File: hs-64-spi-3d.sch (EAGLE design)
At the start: 30 parts, among them J1 DF40C-70DP-0.4V(51), J2 A79622-001, U1 RHD2064_BGA, U2 BNO055, U3 TLV70725

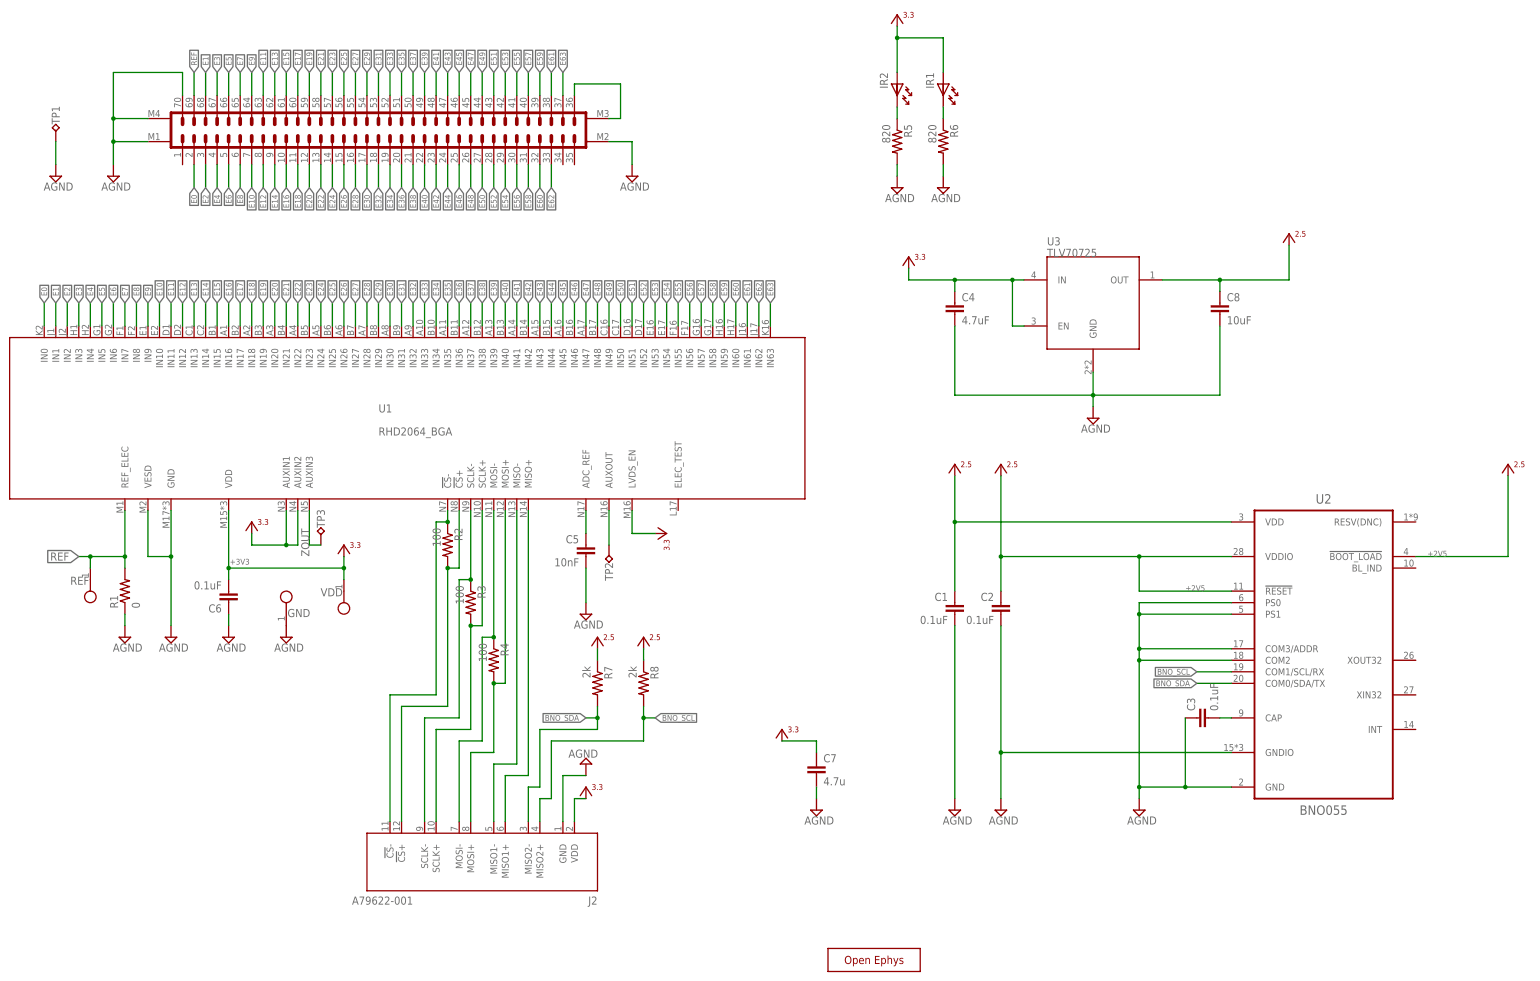
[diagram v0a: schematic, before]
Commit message: Added EEPROM.
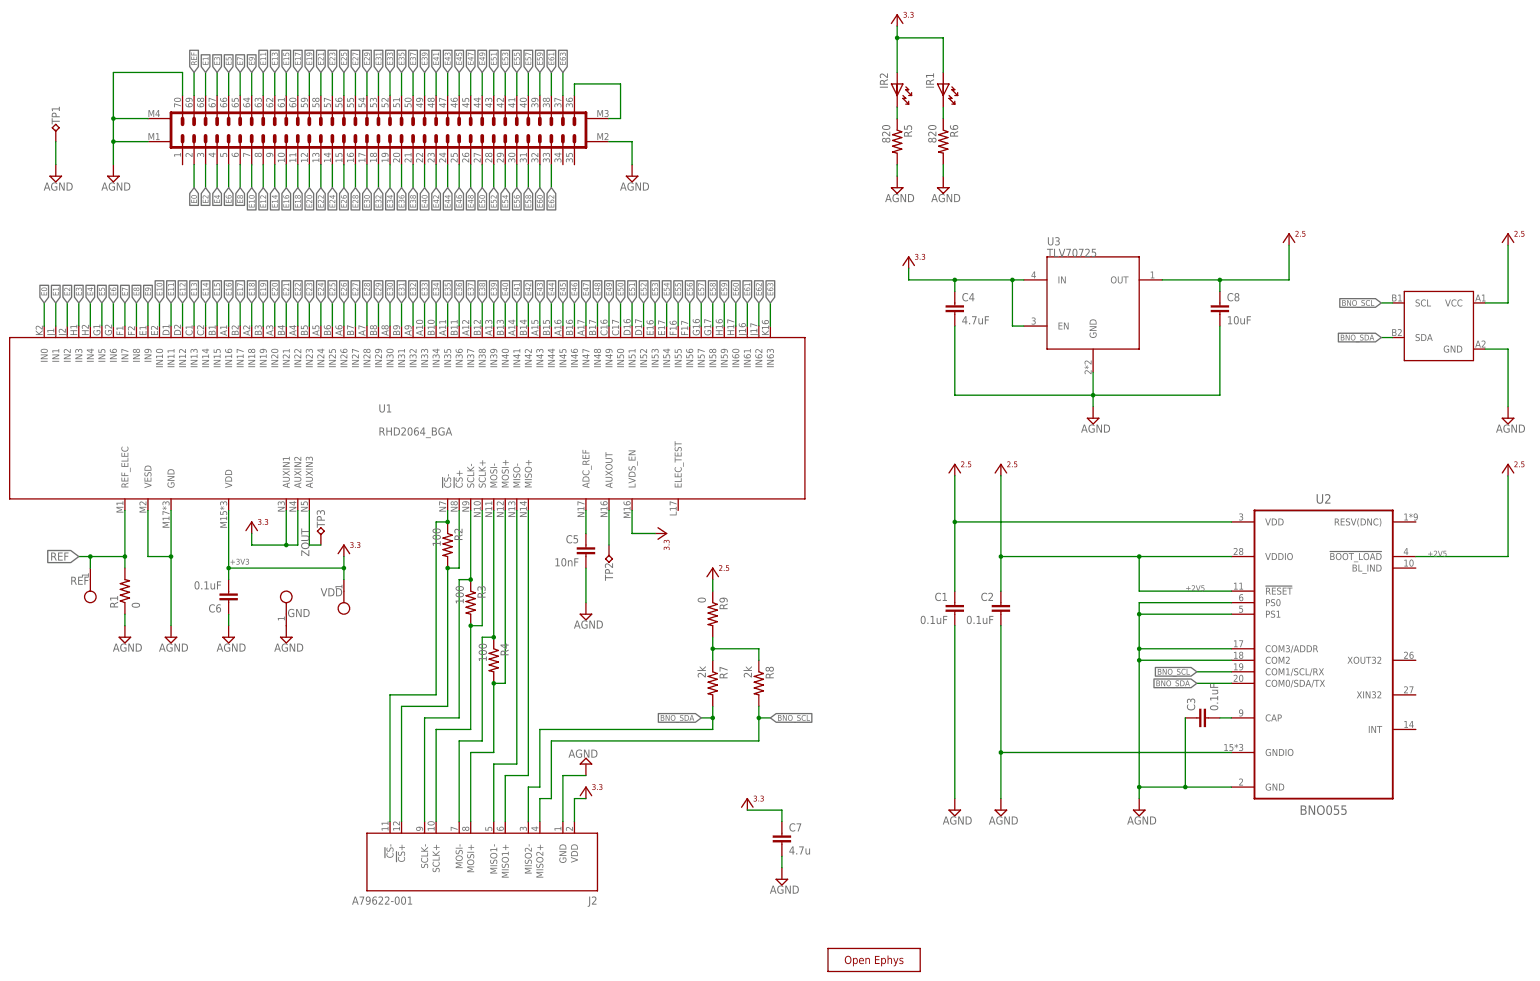
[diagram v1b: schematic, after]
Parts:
- added R9: 0, jonnew:R_0201T
- added U4: 24CW640T-I/CS0668, 24CW640T-I_CS0668:24CW640T-I/CS0668
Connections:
- new net N$1: R7.1, R8.1, R9.2
- net +2V5: now also R9.1, U4.VCC; no longer R7.1, R8.1
- net AGND: now also U4.GND
- net BNO_SCL: now also U4.SCL
- net BNO_SDA: now also U4.SDA
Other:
- moved on the sheet: C7, R7, R8
